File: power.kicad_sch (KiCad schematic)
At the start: 61 parts, among them J3 Conn_02x05_Odd_Even, T1 net-tie, U1 LMR54410, U2 RT9080-33GJ5, U3 TPS546D24ARVFR, U4 MIC5504-MS

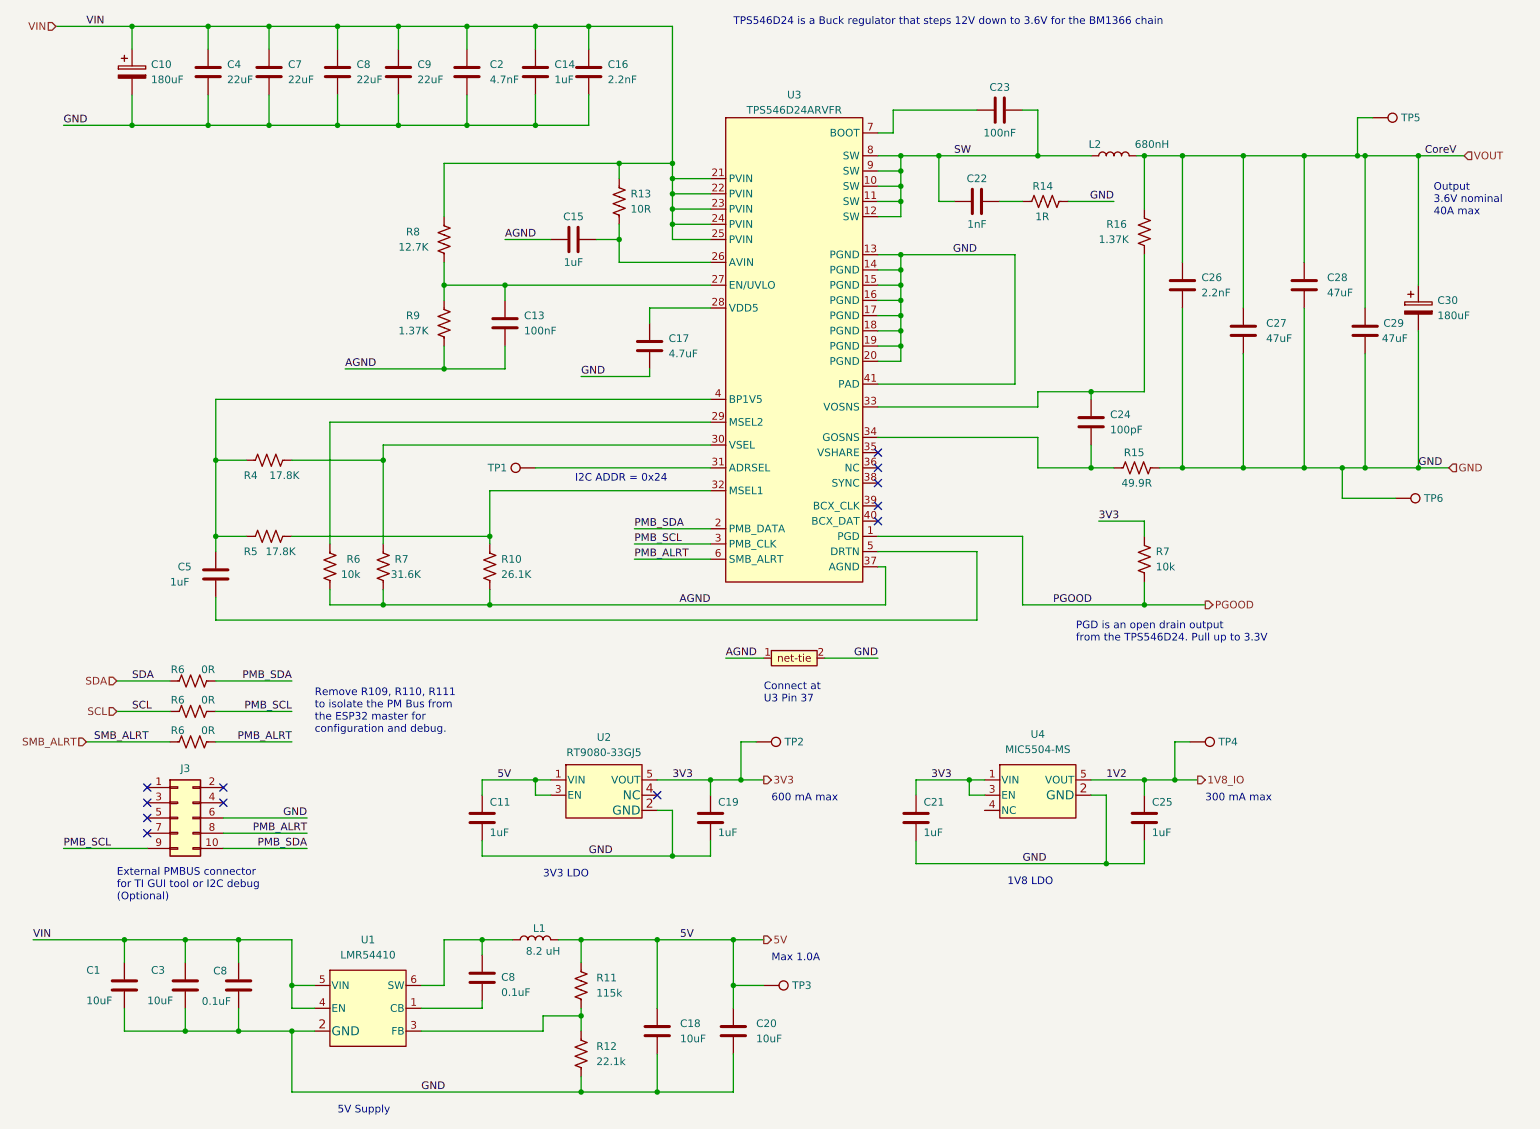
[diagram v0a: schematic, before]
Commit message: -Reset to 1V8/0V8 setup -Add TVS protection
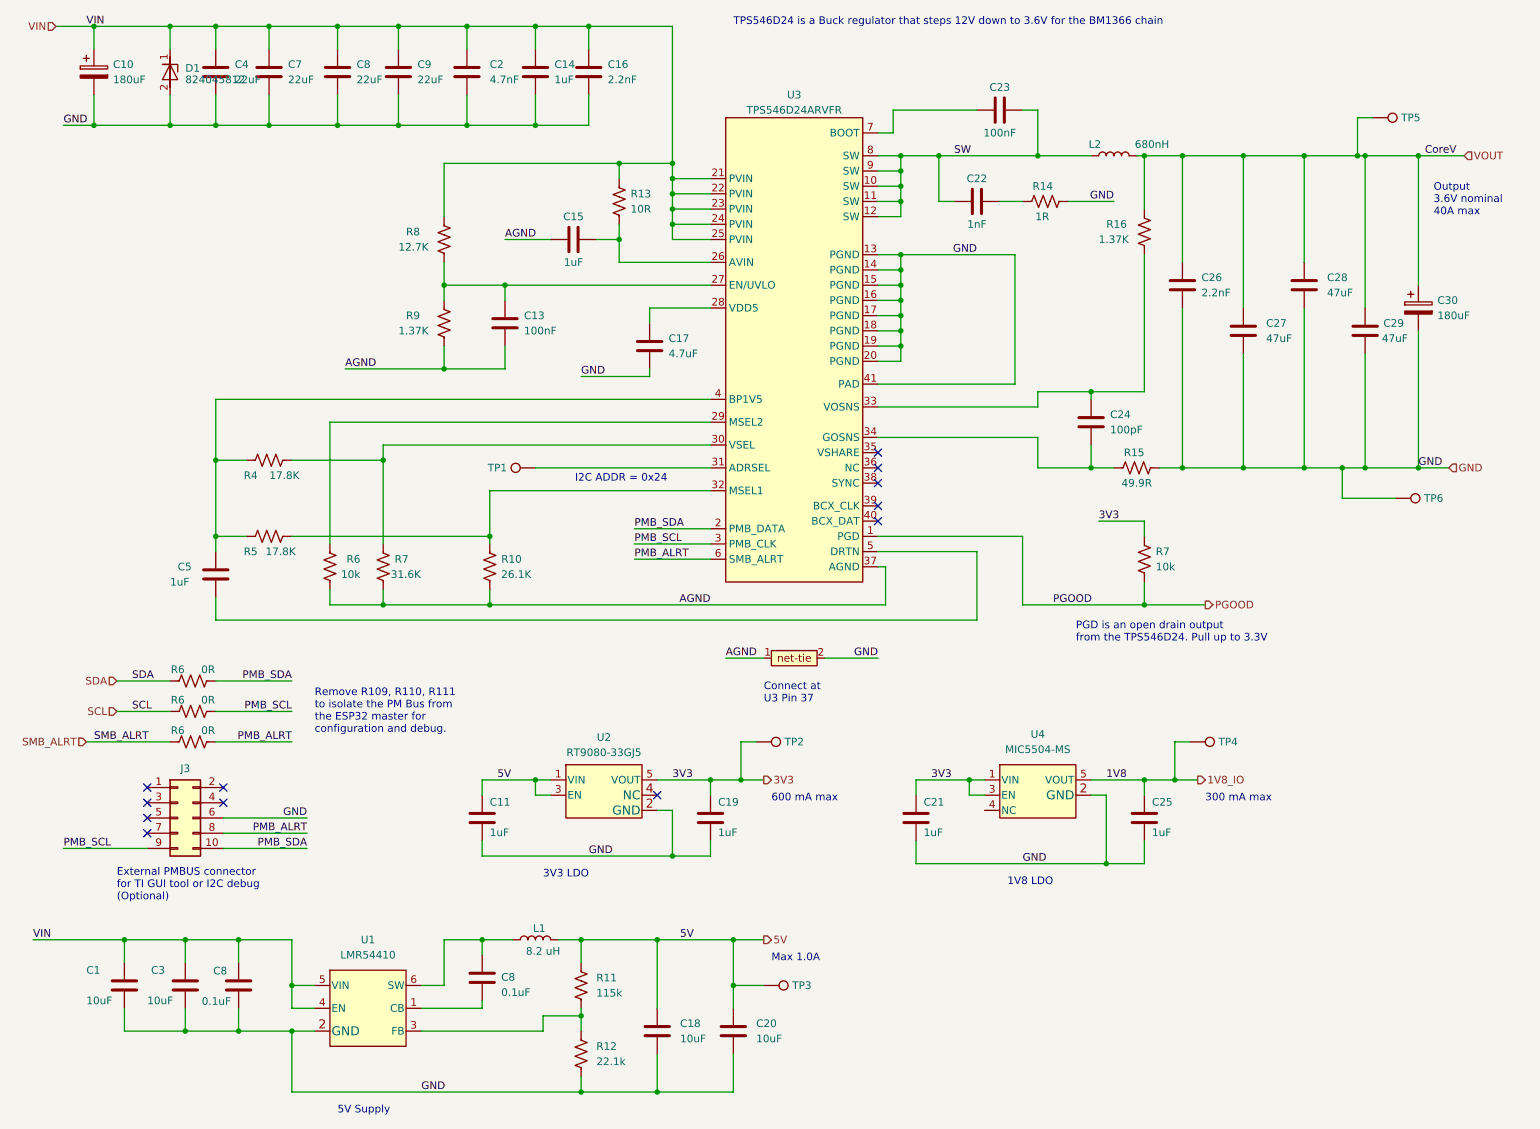
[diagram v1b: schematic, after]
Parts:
- added D1: 824045812, bitaxe:824045812, symbol bitaxe:824045812
- U4: DK C30197547 -> 576-4879-1-ND; PARTNO MIC5504-1.2YM5-TR-MS -> MIC5504-1.8YM5-TR
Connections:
- net GND: now also D1.2 (GND)
- net VIN: now also D1.1 (I/O)
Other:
- moved on the sheet: C10, C4

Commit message: updated to KiCad v9, filled in incomplete BOM and exported.
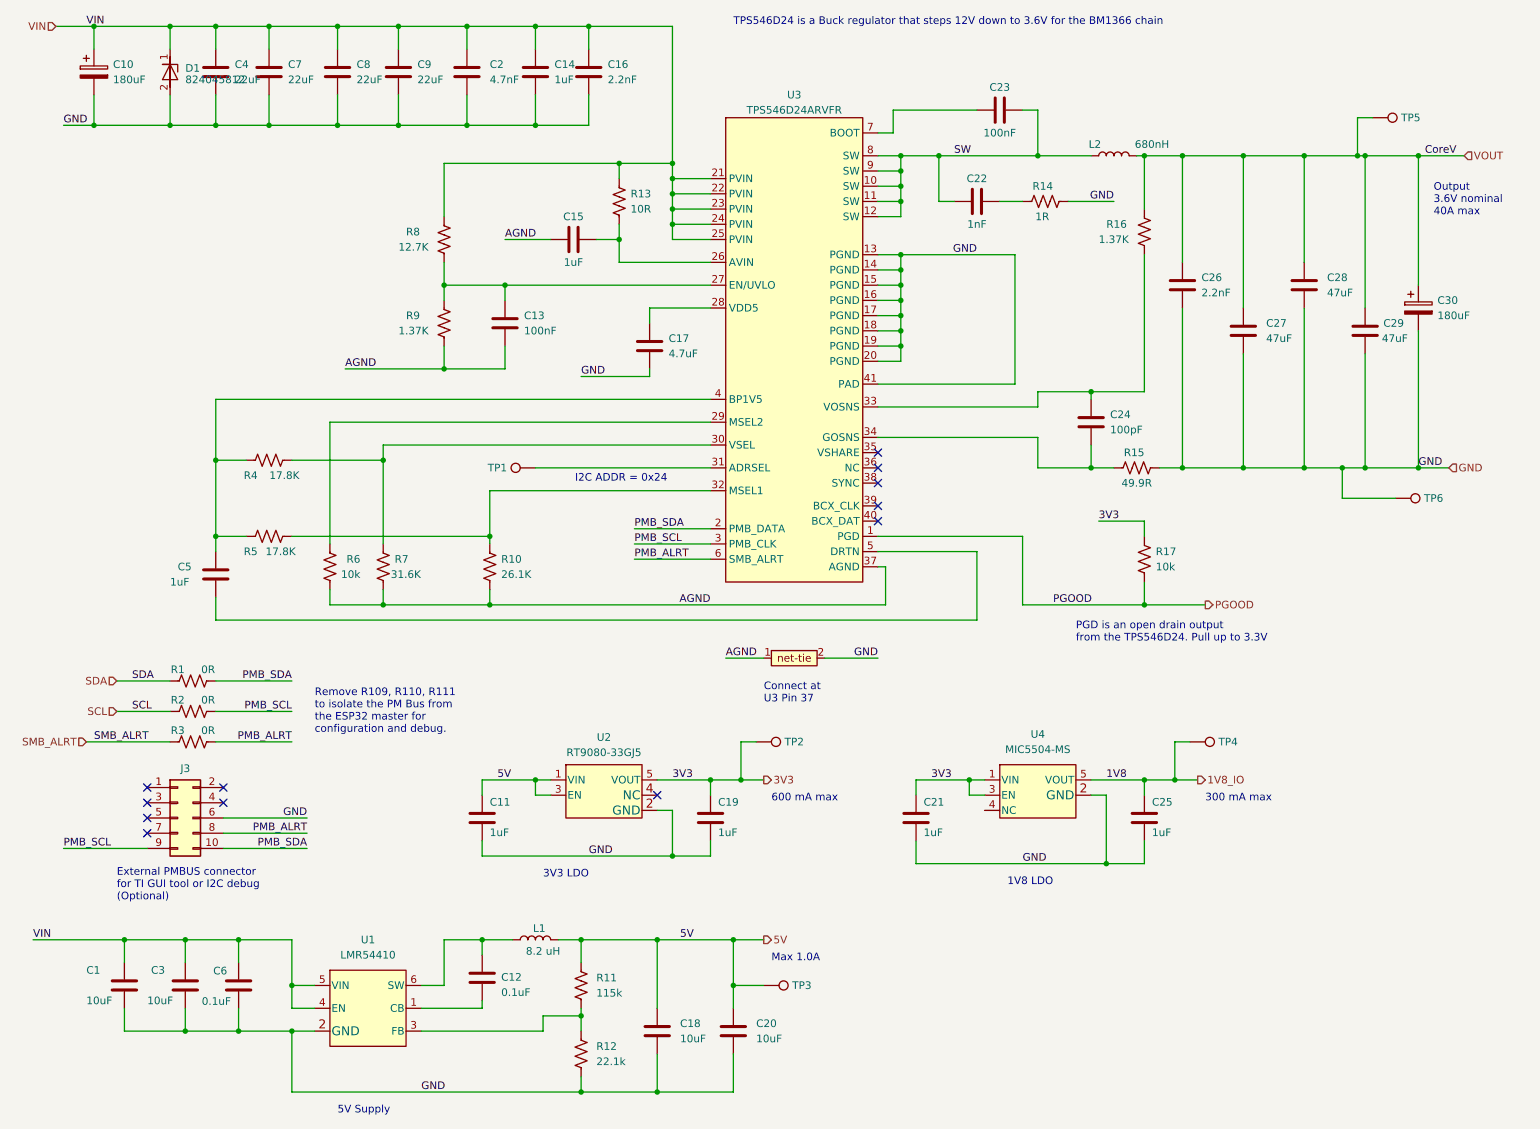
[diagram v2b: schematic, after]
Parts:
- D1: DK (none) -> 732-824045812CT-ND; PARTNO (none) -> 824045812
- renumbered C8 to C12, C8 to C6, R6 to R1, R7 to R17, R6 to R2, R6 to R3
